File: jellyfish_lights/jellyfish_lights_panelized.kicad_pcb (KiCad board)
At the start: 2 copper layers, 94 x 94 mm, 528 parts, among them Q1 AO3400A, SW1 tilt switch, SW2 tilt switch, U1 SN74LVC1G14DBVR

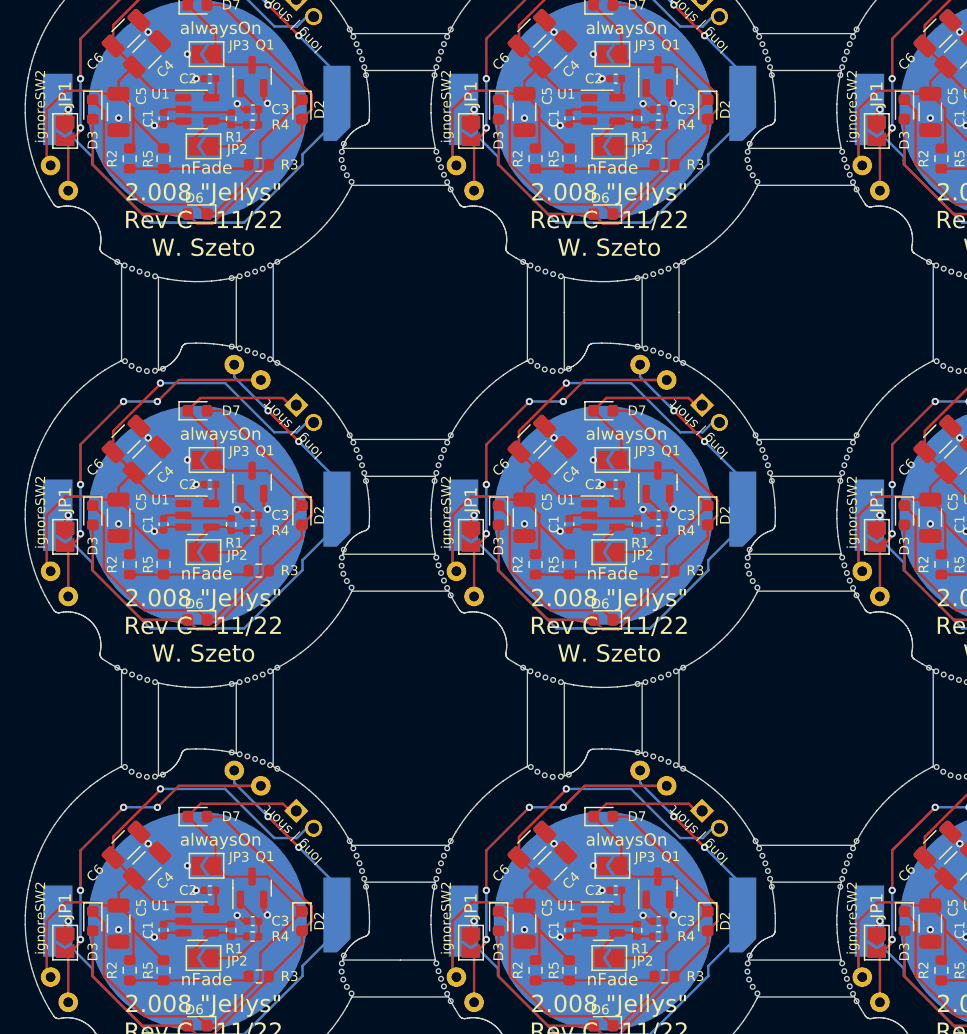
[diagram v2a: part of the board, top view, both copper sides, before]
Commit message: changed jumper to 0R resistor for ignoreSW2
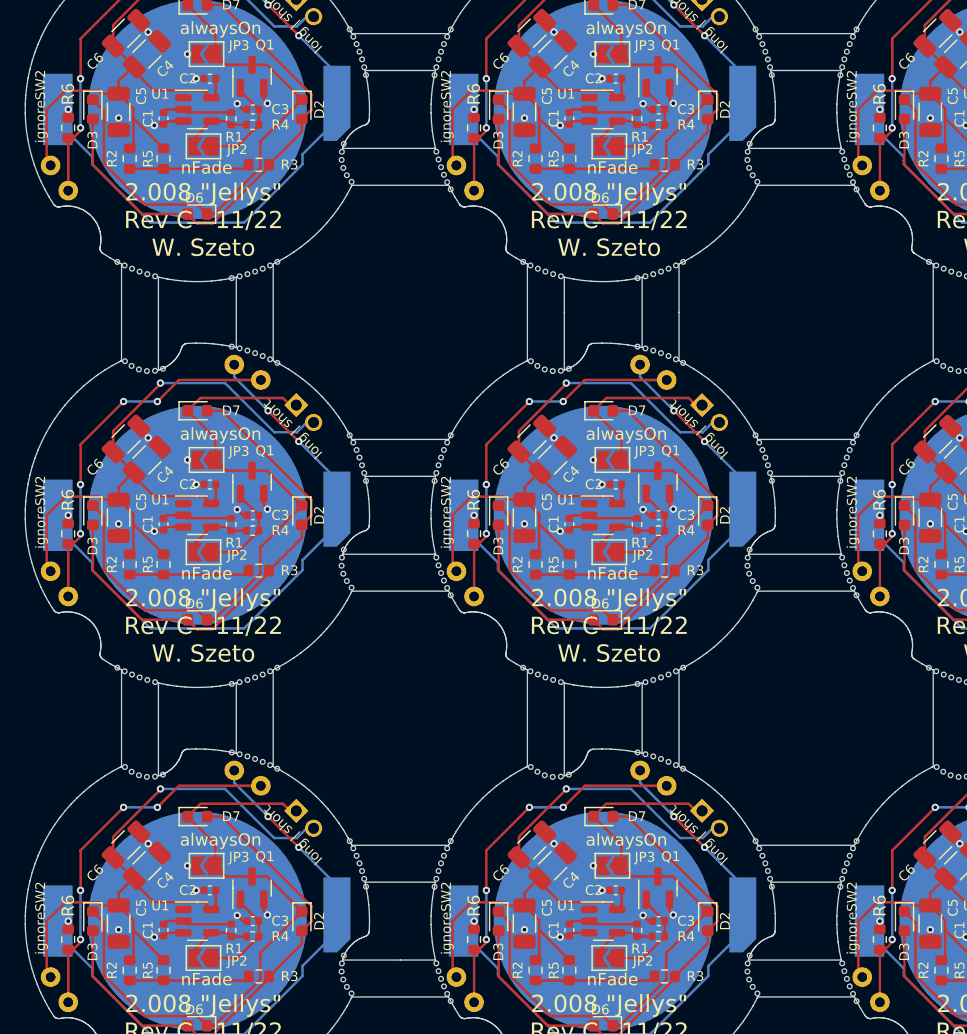
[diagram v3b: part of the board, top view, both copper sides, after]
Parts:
- removed JP1 (x9): oneTiltSw, Jumper:SolderJumper-2_P1.3mm_Open_TrianglePad1.0x1.5mm
- added R6: 0R, Resistor_SMD:R_0603_1608Metric, F.Cu at (72.5, 84.5)
- added R6: 0R, Resistor_SMD:R_0603_1608Metric, F.Cu at (39.5, 84.5)
- added R6: 0R, Resistor_SMD:R_0603_1608Metric, F.Cu at (72.5, 117.5)
- added R6: 0R, Resistor_SMD:R_0603_1608Metric, F.Cu at (105.5, 51.5)
- added R6: 0R, Resistor_SMD:R_0603_1608Metric, F.Cu at (39.5, 117.5)
- added R6: 0R, Resistor_SMD:R_0603_1608Metric, F.Cu at (39.5, 51.5)
- added R6: 0R, Resistor_SMD:R_0603_1608Metric, F.Cu at (105.5, 117.5)
- added R6: 0R, Resistor_SMD:R_0603_1608Metric, F.Cu at (105.5, 84.5)
- added R6: 0R, Resistor_SMD:R_0603_1608Metric, F.Cu at (72.5, 51.5)
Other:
- board text added: "Rev C"

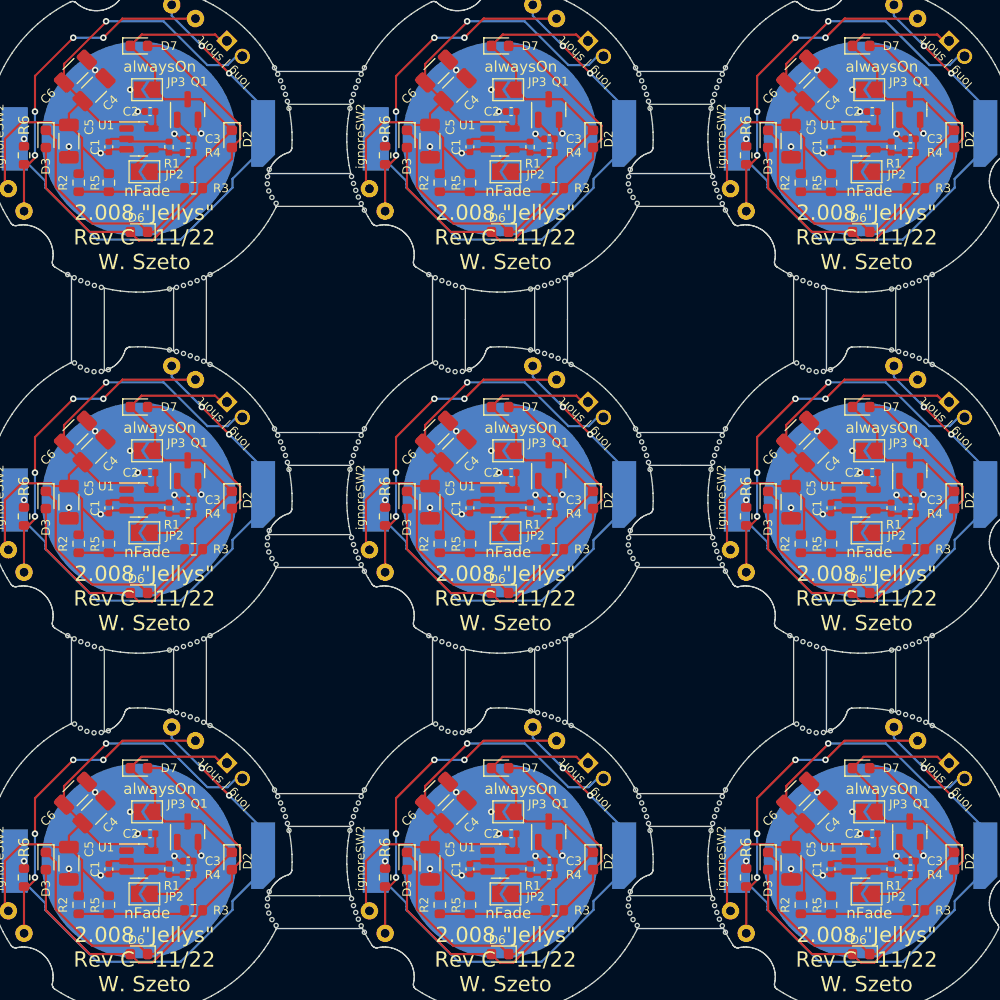
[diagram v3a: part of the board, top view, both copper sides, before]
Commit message: Updated BOM/POS file
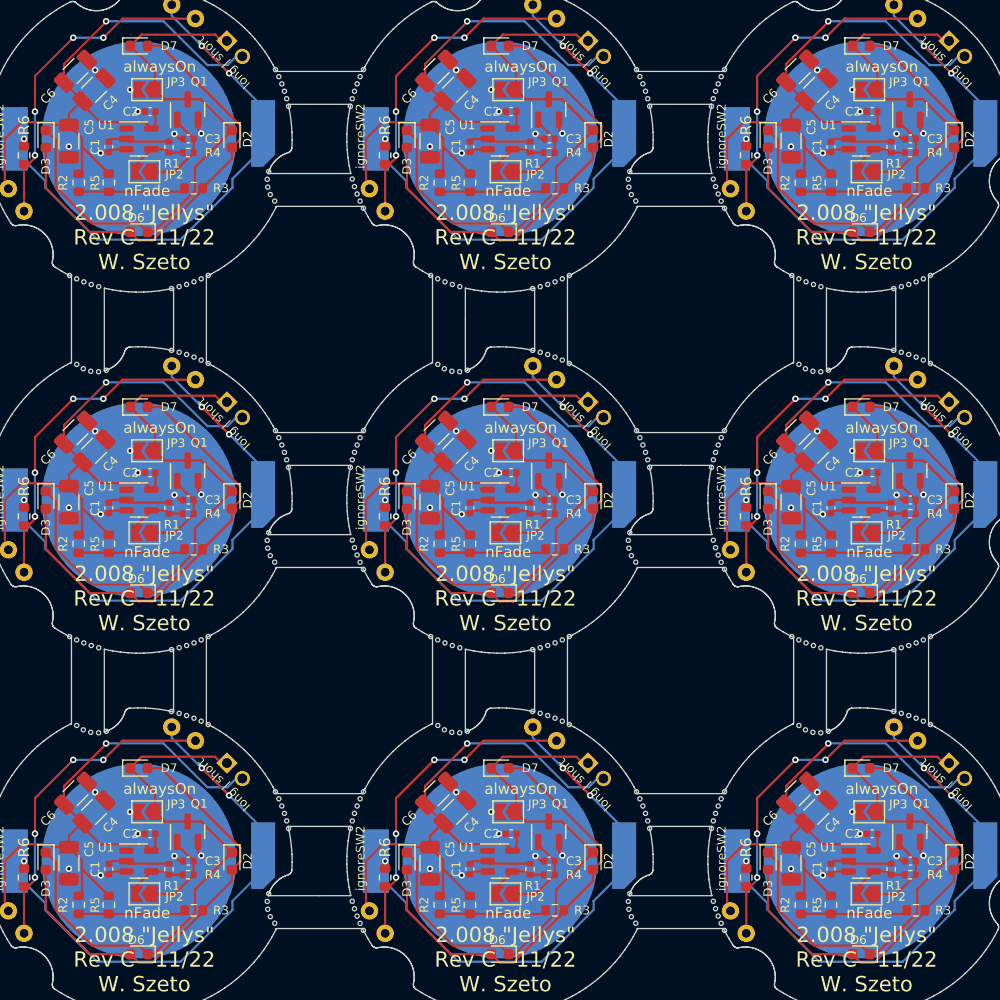
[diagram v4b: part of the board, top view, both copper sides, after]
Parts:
- removed the REF** at (76.5, 62.4)
- removed the REF** at (87.7, 102.8)
- removed the REF** at (121.9, 62.7)
- removed the REF** at (44.1, 70.5)
- removed the REF** at (122.5, 103.6)
- removed the REF** at (118.8, 102.3)
- removed the REF** at (69.6, 45.9)
- removed the REF** at (102.4, 46.6)
- removed the REF** at (119.4, 69.4)
- removed the REF** at (96.2, 111.3)
- removed the REF** at (70.3, 121.9)
- removed the REF** at (102.3, 47.2)
- removed the REF** at (63.4, 45.9)
- removed the REF** at (111.3, 63.2)
- removed the REF** at (78.2, 104.1)
- removed the REF** at (69.3, 80.2)
- removed the REF** at (46.6, 96.6)
- removed the REF** at (78.9, 63.4)
- removed the REF** at (111.9, 104.3)
- removed the REF** at (120.1, 102.6)
- removed the REF** at (96.7, 47.2)
- removed the REF** at (45.9, 96.4)
- removed the REF** at (96.2, 45.3)
- removed the REF** at (86.4, 96.6)
- removed the REF** at (78.3, 96.2)
- removed the REF** at (102.6, 78.9)
- removed the REF** at (118.8, 96.7)
- removed the REF** at (78.9, 96.4)
- removed the REF** at (79.6, 96.6)
- removed the REF** at (96.7, 80.2)
- removed the REF** at (54.7, 63.2)
- removed the REF** at (55.3, 70.1)
- removed the REF** at (87.1, 102.6)
- removed the REF** at (103.3, 77.1)
- removed the REF** at (88.9, 70.3)
- removed the REF** at (61.9, 120.8)
- removed the REF** at (70.6, 76.5)
- removed the REF** at (63.2, 111.3)
- removed the REF** at (94.8, 119.4)
- removed the REF** at (94.9, 87.8)
- removed the REF** at (89.5, 70.6)
- removed the REF** at (63.4, 111.9)
- removed the REF** at (88.3, 70.1)
- removed the REF** at (94.9, 120.8)
- removed the REF** at (94.7, 54.1)
- removed the REF** at (94.9, 85.8)
- removed the REF** at (70.0, 44.7)
- removed the REF** at (70.3, 44.1)
- removed the REF** at (79.6, 63.6)
- removed the REF** at (96.4, 45.9)
- removed the REF** at (103.3, 110.1)
- removed the REF** at (69.8, 54.7)
- removed the REF** at (54.1, 96.4)
- removed the REF** at (61.9, 118.8)
- removed the REF** at (78.2, 71.1)
- removed the REF** at (77.7, 103.9)
- removed the REF** at (52.8, 96.7)
- removed the REF** at (80.2, 71.1)
- removed the REF** at (44.7, 95.9)
- removed the REF** at (103.3, 44.1)
- removed the REF** at (88.3, 103.1)
- removed the REF** at (61.9, 54.8)
- removed the REF** at (95.7, 110.1)
- removed the REF** at (54.1, 69.6)
- removed the REF** at (94.7, 120.1)
- removed the REF** at (44.1, 103.5)
- removed the REF** at (47.2, 71.1)
- removed the REF** at (45.9, 104.3)
- removed the REF** at (61.8, 86.4)
- removed the REF** at (112.6, 104.2)
- removed the REF** at (44.7, 62.9)
- removed the REF** at (109.5, 62.4)
- removed the REF** at (69.6, 87.1)
- removed the REF** at (70.6, 122.5)
- removed the REF** at (122.5, 95.4)
- removed the REF** at (95.2, 121.3)
- removed the REF** at (103.6, 76.5)
- removed the REF** at (69.8, 120.7)
- removed the REF** at (96.6, 46.6)
- removed the REF** at (94.9, 52.8)
- removed the REF** at (96.6, 79.6)
- removed the REF** at (55.9, 70.3)
- removed the REF** at (70.1, 55.3)
- removed the REF** at (61.7, 87.1)
- removed the REF** at (52.8, 63.7)
- removed the REF** at (103.6, 56.5)
- removed the REF** at (45.3, 63.2)
- removed the REF** at (102.6, 54.1)
- removed the REF** at (77.1, 62.7)
- removed the REF** at (45.3, 96.2)
- removed the REF** at (70.6, 43.5)
- removed the REF** at (120.7, 102.8)
- removed the REF** at (103.0, 44.7)
- removed the REF** at (63.2, 78.3)
- removed the REF** at (69.4, 112.6)
- removed the REF** at (61.8, 53.4)
- removed the REF** at (55.9, 103.3)
- removed the REF** at (102.8, 78.3)
- removed the REF** at (54.1, 63.4)
- removed the REF** at (70.1, 88.3)
- removed the REF** at (62.9, 77.7)
- removed the REF** at (85.8, 102.3)
- removed the REF** at (70.3, 88.9)
- removed the REF** at (62.4, 76.5)
- removed the REF** at (78.9, 104.3)
- removed the REF** at (69.3, 113.2)
- removed the REF** at (103.6, 122.5)
- removed the REF** at (96.6, 112.6)
- removed the REF** at (70.3, 77.1)
- removed the REF** at (88.9, 95.7)
- removed the REF** at (45.2, 71.1)
- removed the REF** at (109.5, 95.4)
- removed the REF** at (69.4, 79.6)
- removed the REF** at (69.6, 111.9)
- removed the REF** at (61.9, 87.8)
- removed the REF** at (113.2, 71.1)
- removed the REF** at (120.1, 96.4)
- removed the REF** at (95.5, 55.9)
- removed the REF** at (113.2, 104.1)
- removed the REF** at (69.3, 47.2)
- removed the REF** at (103.0, 77.7)
- removed the REF** at (102.6, 111.9)
- removed the REF** at (111.9, 63.4)
- removed the REF** at (78.3, 63.2)
- removed the REF** at (62.9, 44.7)
- removed the REF** at (95.9, 77.7)
- removed the REF** at (119.4, 63.6)
- removed the REF** at (61.7, 120.1)
- removed the REF** at (95.9, 44.7)
- removed the REF** at (69.4, 53.4)
- removed the REF** at (43.5, 62.4)
- removed the REF** at (77.1, 95.7)
- removed the REF** at (102.8, 45.3)
- removed the REF** at (85.8, 63.7)
- removed the REF** at (103.1, 55.3)
- removed the REF** at (102.8, 54.7)
- removed the REF** at (95.9, 110.7)
- removed the REF** at (56.5, 70.6)
- removed the REF** at (86.4, 63.6)
- removed the REF** at (62.7, 44.1)
- removed the REF** at (96.7, 113.2)
- removed the REF** at (77.7, 70.9)
- removed the REF** at (94.8, 53.4)
- removed the REF** at (102.4, 86.4)
- removed the REF** at (55.3, 96.0)
- removed the REF** at (45.2, 104.1)
- removed the REF** at (86.4, 69.4)
- removed the REF** at (63.2, 45.3)
- removed the REF** at (121.3, 96.0)
- removed the REF** at (56.5, 95.4)
- removed the REF** at (111.9, 96.4)
- removed the REF** at (102.3, 80.2)
- removed the REF** at (112.6, 63.6)
- removed the REF** at (120.7, 96.2)
- removed the REF** at (46.6, 71.2)
- removed the REF** at (103.3, 88.9)
- removed the REF** at (55.9, 62.7)
- removed the REF** at (110.7, 62.9)
- removed the REF** at (95.7, 77.1)
- removed the REF** at (62.7, 110.1)
- removed the REF** at (102.4, 119.4)
- removed the REF** at (54.7, 96.2)
- removed the REF** at (89.5, 95.4)
- removed the REF** at (119.4, 96.6)
- removed the REF** at (102.6, 87.1)
- removed the REF** at (120.1, 69.6)
- removed the REF** at (53.4, 69.4)
- removed the REF** at (111.2, 71.1)
- removed the REF** at (61.7, 54.1)
- removed the REF** at (70.0, 77.7)
- removed the REF** at (112.6, 96.6)
- removed the REF** at (118.8, 69.3)
- removed the REF** at (63.7, 113.2)
- removed the REF** at (69.6, 54.1)
- removed the REF** at (70.6, 89.5)
- removed the REF** at (89.5, 62.4)
- removed the REF** at (77.7, 95.9)
- removed the REF** at (120.7, 63.2)
- removed the REF** at (118.8, 63.7)
- removed the REF** at (52.8, 102.3)
- removed the REF** at (96.4, 78.9)
- removed the REF** at (53.4, 102.4)
- removed the REF** at (63.6, 112.6)
- removed the REF** at (102.4, 53.4)
- removed the REF** at (69.4, 46.6)
- removed the REF** at (119.4, 102.4)
- removed the REF** at (63.6, 46.6)
- removed the REF** at (121.9, 70.3)
- removed the REF** at (53.4, 96.6)
- removed the REF** at (95.4, 109.5)
- removed the REF** at (69.4, 86.4)
- removed the REF** at (53.4, 63.6)
- removed the REF** at (103.1, 88.3)
- removed the REF** at (78.9, 71.3)
- removed the REF** at (95.4, 76.5)
- removed the REF** at (69.6, 120.1)
- removed the REF** at (62.2, 55.3)
- removed the REF** at (63.4, 78.9)
- removed the REF** at (121.3, 70.1)
- removed the REF** at (69.8, 87.7)
- removed the REF** at (63.6, 79.6)
- removed the REF** at (45.9, 63.4)
- removed the REF** at (70.6, 109.5)
- removed the REF** at (80.2, 104.1)
- removed the REF** at (96.2, 78.3)
- removed the REF** at (46.6, 63.6)
- removed the REF** at (110.7, 95.9)
- removed the REF** at (44.1, 62.7)
- removed the REF** at (103.6, 43.5)
- removed the REF** at (46.6, 104.2)
- removed the REF** at (76.5, 95.4)
- removed the REF** at (103.3, 55.9)
- removed the REF** at (94.7, 87.1)
- removed the REF** at (102.4, 112.6)
- removed the REF** at (87.7, 96.2)
- removed the REF** at (89.5, 103.6)
- removed the REF** at (103.1, 121.3)
- removed the REF** at (87.1, 69.6)
- removed the REF** at (87.1, 96.4)
- removed the REF** at (69.8, 78.3)
- removed the REF** at (122.5, 70.6)
- removed the REF** at (44.1, 95.7)
- removed the REF** at (77.7, 62.9)
- removed the REF** at (56.5, 103.6)
- removed the REF** at (54.1, 102.6)
- removed the REF** at (87.7, 69.8)
- removed the REF** at (102.8, 87.7)
- removed the REF** at (102.6, 45.9)
- removed the REF** at (77.1, 70.5)
- removed the REF** at (94.9, 54.8)
- removed the REF** at (95.7, 44.1)
- removed the REF** at (102.4, 79.6)
- removed the REF** at (94.8, 86.4)
- removed the REF** at (95.5, 121.9)
- removed the REF** at (88.3, 63.0)
- removed the REF** at (121.3, 103.1)
- removed the REF** at (95.2, 55.3)
- removed the REF** at (55.9, 95.7)
- removed the REF** at (61.9, 85.8)
- removed the REF** at (70.6, 56.5)
- removed the REF** at (102.6, 120.1)
- removed the REF** at (61.8, 119.4)
- removed the REF** at (121.9, 95.7)
- removed the REF** at (85.8, 96.7)
- removed the REF** at (62.2, 88.3)
- removed the REF** at (110.7, 70.9)
- removed the REF** at (62.9, 110.7)
- removed the REF** at (88.3, 96.0)
- removed the REF** at (88.9, 103.3)
- removed the REF** at (61.9, 52.8)
- removed the REF** at (87.7, 63.2)
- removed the REF** at (111.3, 96.2)
- removed the REF** at (111.2, 104.1)
- removed the REF** at (79.6, 104.2)
- removed the REF** at (102.8, 111.3)
- removed the REF** at (102.8, 120.7)
- removed the REF** at (62.5, 55.9)
- removed the REF** at (95.4, 43.5)
- removed the REF** at (69.6, 78.9)
- removed the REF** at (62.7, 77.1)
- removed the REF** at (103.0, 110.7)
- removed the REF** at (102.3, 113.2)
- removed the REF** at (95.5, 88.9)
- removed the REF** at (95.2, 88.3)
- removed the REF** at (85.8, 69.3)
- removed the REF** at (44.7, 70.9)
- removed the REF** at (55.3, 63.0)
- removed the REF** at (96.4, 111.9)
- removed the REF** at (55.3, 103.1)
- removed the REF** at (70.0, 110.7)
- removed the REF** at (70.1, 121.3)
- removed the REF** at (44.7, 103.9)
- removed the REF** at (88.9, 62.7)
- removed the REF** at (62.2, 121.3)
- removed the REF** at (103.3, 121.9)
- removed the REF** at (110.1, 103.5)
- removed the REF** at (47.2, 104.1)
- removed the REF** at (110.1, 70.5)
- removed the REF** at (110.1, 95.7)
- removed the REF** at (62.5, 121.9)
- removed the REF** at (121.3, 63.0)
- removed the REF** at (87.1, 63.4)
- removed the REF** at (69.8, 45.3)
- removed the REF** at (43.5, 95.4)
- removed the REF** at (70.3, 55.9)
- removed the REF** at (70.3, 110.1)
- removed the REF** at (63.7, 47.2)
- removed the REF** at (63.7, 80.2)
- removed the REF** at (110.7, 103.9)
- removed the REF** at (94.9, 118.8)
- removed the REF** at (111.9, 71.3)
- removed the REF** at (52.8, 69.3)
- removed the REF** at (120.7, 69.8)
- removed the REF** at (45.9, 71.3)
- removed the REF** at (79.6, 71.2)
- removed the REF** at (69.4, 119.4)
- removed the REF** at (86.4, 102.4)
- removed the REF** at (120.1, 63.4)
- removed the REF** at (56.5, 62.4)
- removed the REF** at (54.7, 69.8)
- removed the REF** at (62.5, 88.9)
- removed the REF** at (103.6, 89.5)
- removed the REF** at (110.1, 62.7)
- removed the REF** at (103.6, 109.5)
- removed the REF** at (121.9, 103.3)
- removed the REF** at (122.5, 62.4)
- removed the REF** at (62.4, 109.5)
- removed the REF** at (62.4, 43.5)
- removed the REF** at (112.6, 71.2)
- removed the REF** at (77.1, 103.5)
- removed the REF** at (54.7, 102.8)
- removed the REF** at (69.8, 111.3)
- added REF**: NPTH, NPTH, F.Cu at (103.2, 110.3)
- added REF**: NPTH, NPTH, F.Cu at (95.5, 76.7)
- added REF**: NPTH, NPTH, F.Cu at (113.0, 71.1)
- added REF**: NPTH, NPTH, F.Cu at (79.3, 104.3)
- added REF**: NPTH, NPTH, F.Cu at (61.8, 87.4)
- added REF**: NPTH, NPTH, F.Cu at (102.7, 45.6)
- added REF**: NPTH, NPTH, F.Cu at (69.7, 111.6)
- added REF**: NPTH, NPTH, F.Cu at (45.6, 71.2)
- added REF**: NPTH, NPTH, F.Cu at (80.0, 104.1)
- added REF**: NPTH, NPTH, F.Cu at (121.0, 63.1)
- added REF**: NPTH, NPTH, F.Cu at (70.2, 55.7)
- added REF**: NPTH, NPTH, F.Cu at (43.7, 62.5)
- added REF**: NPTH, NPTH, F.Cu at (44.3, 62.8)
- added REF**: NPTH, NPTH, F.Cu at (102.9, 55.0)
- added REF**: NPTH, NPTH, F.Cu at (70.5, 122.3)
- added REF**: NPTH, NPTH, F.Cu at (86.7, 96.5)
- added REF**: NPTH, NPTH, F.Cu at (121.7, 62.8)
- added REF**: NPTH, NPTH, F.Cu at (63.5, 79.3)
- added REF**: NPTH, NPTH, F.Cu at (96.3, 78.6)
- added REF**: NPTH, NPTH, F.Cu at (96.3, 45.6)
- added REF**: NPTH, NPTH, F.Cu at (63.7, 113.0)
- added REF**: NPTH, NPTH, F.Cu at (110.9, 104.0)
- added REF**: NPTH, NPTH, F.Cu at (119.7, 96.5)
- added REF**: NPTH, NPTH, F.Cu at (94.8, 54.4)
- added REF**: NPTH, NPTH, F.Cu at (87.4, 63.3)
- added REF**: NPTH, NPTH, F.Cu at (87.4, 96.3)
- added REF**: NPTH, NPTH, F.Cu at (102.3, 47.0)
- added REF**: NPTH, NPTH, F.Cu at (96.5, 79.3)
- added REF**: NPTH, NPTH, F.Cu at (89.3, 103.5)
- added REF**: NPTH, NPTH, F.Cu at (102.7, 54.4)
- added REF**: NPTH, NPTH, F.Cu at (102.9, 45.0)
- added REF**: NPTH, NPTH, F.Cu at (95.5, 43.7)
- added REF**: NPTH, NPTH, F.Cu at (70.2, 121.7)
- added REF**: NPTH, NPTH, F.Cu at (77.9, 71.0)
- added REF**: NPTH, NPTH, F.Cu at (62.5, 76.7)
- added REF**: NPTH, NPTH, F.Cu at (89.3, 62.5)
- added REF**: NPTH, NPTH, F.Cu at (53.7, 96.5)
- added REF**: NPTH, NPTH, F.Cu at (102.5, 79.3)
- added REF**: NPTH, NPTH, F.Cu at (95.8, 77.3)
- added REF**: NPTH, NPTH, F.Cu at (63.7, 47.0)
- added REF**: NPTH, NPTH, F.Cu at (70.2, 110.3)
- added REF**: NPTH, NPTH, F.Cu at (55.7, 70.2)
- added REF**: NPTH, NPTH, F.Cu at (95.8, 110.3)
- added REF**: NPTH, NPTH, F.Cu at (46.3, 63.5)
- added REF**: NPTH, NPTH, F.Cu at (103.5, 76.7)
- added REF**: NPTH, NPTH, F.Cu at (96.7, 47.0)
- added REF**: NPTH, NPTH, F.Cu at (69.9, 111.0)
- added REF**: NPTH, NPTH, F.Cu at (78.6, 96.3)
- added REF**: NPTH, NPTH, F.Cu at (53.7, 63.5)
- added REF**: NPTH, NPTH, F.Cu at (69.3, 80.0)
- added REF**: NPTH, NPTH, F.Cu at (79.3, 96.5)
- added REF**: NPTH, NPTH, F.Cu at (69.9, 55.0)
- added REF**: NPTH, NPTH, F.Cu at (111.6, 104.2)
- added REF**: NPTH, NPTH, F.Cu at (45.6, 96.3)
- added REF**: NPTH, NPTH, F.Cu at (121.0, 96.1)
- added REF**: NPTH, NPTH, F.Cu at (62.8, 77.3)
- added REF**: NPTH, NPTH, F.Cu at (111.6, 96.3)
- added REF**: NPTH, NPTH, F.Cu at (62.4, 88.7)
- added REF**: NPTH, NPTH, F.Cu at (121.7, 95.8)
- added REF**: NPTH, NPTH, F.Cu at (69.5, 53.7)
- added REF**: NPTH, NPTH, F.Cu at (77.3, 103.6)
- added REF**: NPTH, NPTH, F.Cu at (96.1, 78.0)
- added REF**: NPTH, NPTH, F.Cu at (78.0, 63.1)
- added REF**: NPTH, NPTH, F.Cu at (54.4, 102.7)
- added REF**: NPTH, NPTH, F.Cu at (121.7, 70.2)
- added REF**: NPTH, NPTH, F.Cu at (54.4, 96.3)
- added REF**: NPTH, NPTH, F.Cu at (88.7, 95.8)
- added REF**: NPTH, NPTH, F.Cu at (43.7, 95.5)
- added REF**: NPTH, NPTH, F.Cu at (61.9, 53.0)
- added REF**: NPTH, NPTH, F.Cu at (55.0, 102.9)
- added REF**: NPTH, NPTH, F.Cu at (61.8, 54.4)
- added REF**: NPTH, NPTH, F.Cu at (53.0, 96.7)
- added REF**: NPTH, NPTH, F.Cu at (62.4, 55.7)
- added REF**: NPTH, NPTH, F.Cu at (103.5, 89.3)
- added REF**: NPTH, NPTH, F.Cu at (119.7, 69.5)
- added REF**: NPTH, NPTH, F.Cu at (69.5, 46.3)
- added REF**: NPTH, NPTH, F.Cu at (110.3, 95.8)
- added REF**: NPTH, NPTH, F.Cu at (88.0, 96.1)
- added REF**: NPTH, NPTH, F.Cu at (70.5, 76.7)
- added REF**: NPTH, NPTH, F.Cu at (102.3, 80.0)
- added REF**: NPTH, NPTH, F.Cu at (70.2, 44.3)
- added REF**: NPTH, NPTH, F.Cu at (119.0, 69.3)
- added REF**: NPTH, NPTH, F.Cu at (94.9, 53.0)
- added REF**: NPTH, NPTH, F.Cu at (63.1, 111.0)
- added REF**: NPTH, NPTH, F.Cu at (46.3, 71.3)
- added REF**: NPTH, NPTH, F.Cu at (76.7, 62.5)
- added REF**: NPTH, NPTH, F.Cu at (63.3, 111.6)
- added REF**: NPTH, NPTH, F.Cu at (119.0, 102.3)
- added REF**: NPTH, NPTH, F.Cu at (76.7, 95.5)
- added REF**: NPTH, NPTH, F.Cu at (96.1, 111.0)
- added REF**: NPTH, NPTH, F.Cu at (110.3, 103.6)
- added REF**: NPTH, NPTH, F.Cu at (78.6, 104.2)
- added REF**: NPTH, NPTH, F.Cu at (45.0, 96.1)
- added REF**: NPTH, NPTH, F.Cu at (45.0, 63.1)
- added REF**: NPTH, NPTH, F.Cu at (121.7, 103.2)
- added REF**: NPTH, NPTH, F.Cu at (87.4, 69.7)
- added REF**: NPTH, NPTH, F.Cu at (77.3, 62.8)
- added REF**: NPTH, NPTH, F.Cu at (53.0, 69.3)
- added REF**: NPTH, NPTH, F.Cu at (62.0, 88.1)
- added REF**: NPTH, NPTH, F.Cu at (77.3, 95.8)
- added REF**: NPTH, NPTH, F.Cu at (94.9, 119.0)
- added REF**: NPTH, NPTH, F.Cu at (63.5, 112.3)
- added REF**: NPTH, NPTH, F.Cu at (69.9, 121.0)
- added REF**: NPTH, NPTH, F.Cu at (78.6, 71.2)
- added REF**: NPTH, NPTH, F.Cu at (55.7, 95.8)
- added REF**: NPTH, NPTH, F.Cu at (70.5, 56.3)
- added REF**: NPTH, NPTH, F.Cu at (62.0, 55.1)
- added REF**: NPTH, NPTH, F.Cu at (103.2, 88.7)
- added REF**: NPTH, NPTH, F.Cu at (119.7, 63.5)
- added REF**: NPTH, NPTH, F.Cu at (78.0, 96.1)
- added REF**: NPTH, NPTH, F.Cu at (88.0, 69.9)
- added REF**: NPTH, NPTH, F.Cu at (110.3, 62.8)
- added REF**: NPTH, NPTH, F.Cu at (103.5, 122.3)
- added REF**: NPTH, NPTH, F.Cu at (94.9, 86.0)
- added REF**: NPTH, NPTH, F.Cu at (88.0, 102.9)
- added REF**: NPTH, NPTH, F.Cu at (69.9, 78.0)
- added REF**: NPTH, NPTH, F.Cu at (86.7, 63.5)
- added REF**: NPTH, NPTH, F.Cu at (119.7, 102.5)
- added REF**: NPTH, NPTH, F.Cu at (96.5, 112.3)
- added REF**: NPTH, NPTH, F.Cu at (69.7, 120.4)
- added REF**: NPTH, NPTH, F.Cu at (62.8, 110.3)
- added REF**: NPTH, NPTH, F.Cu at (69.5, 79.3)
- added REF**: NPTH, NPTH, F.Cu at (95.0, 121.1)
- added REF**: NPTH, NPTH, F.Cu at (56.3, 70.5)
- added REF**: NPTH, NPTH, F.Cu at (79.3, 63.5)
- added REF**: NPTH, NPTH, F.Cu at (110.9, 71.0)
- added REF**: NPTH, NPTH, F.Cu at (61.8, 120.4)
- added REF**: NPTH, NPTH, F.Cu at (96.7, 113.0)
- added REF**: NPTH, NPTH, F.Cu at (102.7, 87.4)
- added REF**: NPTH, NPTH, F.Cu at (69.5, 86.7)
- added REF**: NPTH, NPTH, F.Cu at (89.3, 70.5)
- added REF**: NPTH, NPTH, F.Cu at (95.4, 88.7)
- added REF**: NPTH, NPTH, F.Cu at (44.3, 103.6)
- added REF**: NPTH, NPTH, F.Cu at (102.5, 112.3)
- added REF**: NPTH, NPTH, F.Cu at (86.0, 96.7)
- added REF**: NPTH, NPTH, F.Cu at (111.0, 63.1)
- added REF**: NPTH, NPTH, F.Cu at (44.3, 95.8)
- added REF**: NPTH, NPTH, F.Cu at (88.0, 63.1)
- added REF**: NPTH, NPTH, F.Cu at (61.7, 53.7)
- added REF**: NPTH, NPTH, F.Cu at (70.5, 109.7)
- added REF**: NPTH, NPTH, F.Cu at (96.1, 45.0)
- added REF**: NPTH, NPTH, F.Cu at (69.3, 113.0)
- added REF**: NPTH, NPTH, F.Cu at (45.6, 104.2)
- added REF**: NPTH, NPTH, F.Cu at (110.3, 70.6)
- added REF**: NPTH, NPTH, F.Cu at (88.7, 62.8)
- added REF**: NPTH, NPTH, F.Cu at (61.9, 119.0)
- added REF**: NPTH, NPTH, F.Cu at (102.5, 86.7)
- added REF**: NPTH, NPTH, F.Cu at (112.3, 71.3)
- added REF**: NPTH, NPTH, F.Cu at (55.0, 69.9)
- added REF**: NPTH, NPTH, F.Cu at (96.5, 46.3)
- added REF**: NPTH, NPTH, F.Cu at (95.4, 121.7)
- added REF**: NPTH, NPTH, F.Cu at (44.9, 71.0)
- added REF**: NPTH, NPTH, F.Cu at (102.7, 111.6)
- added REF**: NPTH, NPTH, F.Cu at (102.5, 46.3)
- added REF**: NPTH, NPTH, F.Cu at (102.3, 113.0)
- added REF**: NPTH, NPTH, F.Cu at (54.4, 63.3)
- added REF**: NPTH, NPTH, F.Cu at (120.4, 96.3)
- added REF**: NPTH, NPTH, F.Cu at (63.3, 45.6)
- added REF**: NPTH, NPTH, F.Cu at (69.7, 45.6)
- added REF**: NPTH, NPTH, F.Cu at (111.0, 96.1)
- added REF**: NPTH, NPTH, F.Cu at (121.0, 102.9)
- added REF**: NPTH, NPTH, F.Cu at (94.8, 87.4)
- added REF**: NPTH, NPTH, F.Cu at (87.4, 102.7)
- added REF**: NPTH, NPTH, F.Cu at (109.7, 62.5)
- added REF**: NPTH, NPTH, F.Cu at (86.0, 102.3)
- added REF**: NPTH, NPTH, F.Cu at (88.7, 103.2)
- added REF**: NPTH, NPTH, F.Cu at (56.3, 62.5)
- added REF**: NPTH, NPTH, F.Cu at (69.9, 88.0)
- added REF**: NPTH, NPTH, F.Cu at (120.4, 63.3)
- added REF**: NPTH, NPTH, F.Cu at (103.2, 121.7)
- added REF**: NPTH, NPTH, F.Cu at (44.9, 104.0)
- added REF**: NPTH, NPTH, F.Cu at (120.4, 102.7)
- added REF**: NPTH, NPTH, F.Cu at (95.5, 109.7)
- added REF**: NPTH, NPTH, F.Cu at (103.5, 56.3)
- added REF**: NPTH, NPTH, F.Cu at (69.5, 112.3)
- added REF**: NPTH, NPTH, F.Cu at (77.9, 104.0)
- added REF**: NPTH, NPTH, F.Cu at (94.7, 119.7)
- added REF**: NPTH, NPTH, F.Cu at (79.3, 71.3)
- added REF**: NPTH, NPTH, F.Cu at (46.3, 96.5)
- added REF**: NPTH, NPTH, F.Cu at (56.3, 95.5)
- added REF**: NPTH, NPTH, F.Cu at (95.4, 55.7)
- added REF**: NPTH, NPTH, F.Cu at (103.2, 77.3)
- added REF**: NPTH, NPTH, F.Cu at (69.7, 87.4)
- added REF**: NPTH, NPTH, F.Cu at (102.5, 53.7)
- added REF**: NPTH, NPTH, F.Cu at (102.7, 120.4)
- added REF**: NPTH, NPTH, F.Cu at (63.5, 46.3)
- added REF**: NPTH, NPTH, F.Cu at (112.3, 63.5)
- added REF**: NPTH, NPTH, F.Cu at (111.6, 63.3)
- added REF**: NPTH, NPTH, F.Cu at (56.3, 103.5)
- added REF**: NPTH, NPTH, F.Cu at (102.7, 78.6)
- added REF**: NPTH, NPTH, F.Cu at (63.7, 80.0)
- added REF**: NPTH, NPTH, F.Cu at (112.3, 96.5)
- added REF**: NPTH, NPTH, F.Cu at (53.0, 102.3)
- added REF**: NPTH, NPTH, F.Cu at (102.9, 121.0)
- added REF**: NPTH, NPTH, F.Cu at (119.0, 96.7)
- added REF**: NPTH, NPTH, F.Cu at (53.7, 102.5)
- added REF**: NPTH, NPTH, F.Cu at (86.0, 69.3)
- added REF**: NPTH, NPTH, F.Cu at (62.5, 43.7)
- added REF**: NPTH, NPTH, F.Cu at (46.3, 104.3)
- added REF**: NPTH, NPTH, F.Cu at (102.9, 78.0)
- added REF**: NPTH, NPTH, F.Cu at (103.5, 43.7)
- added REF**: NPTH, NPTH, F.Cu at (88.7, 70.2)
- added REF**: NPTH, NPTH, F.Cu at (62.8, 44.3)
- added REF**: NPTH, NPTH, F.Cu at (95.0, 88.1)
- added REF**: NPTH, NPTH, F.Cu at (55.7, 62.8)
- added REF**: NPTH, NPTH, F.Cu at (70.2, 88.7)
- added REF**: NPTH, NPTH, F.Cu at (69.7, 78.6)
- added REF**: NPTH, NPTH, F.Cu at (47.0, 71.1)
- added REF**: NPTH, NPTH, F.Cu at (122.3, 103.5)
- added REF**: NPTH, NPTH, F.Cu at (54.4, 69.7)
- added REF**: NPTH, NPTH, F.Cu at (55.0, 96.1)
- added REF**: NPTH, NPTH, F.Cu at (113.0, 104.1)
- added REF**: NPTH, NPTH, F.Cu at (120.4, 69.7)
- added REF**: NPTH, NPTH, F.Cu at (63.3, 78.6)
- added REF**: NPTH, NPTH, F.Cu at (47.0, 104.1)
- added REF**: NPTH, NPTH, F.Cu at (94.7, 86.7)
- added REF**: NPTH, NPTH, F.Cu at (122.3, 62.5)
- added REF**: NPTH, NPTH, F.Cu at (55.7, 103.2)
- added REF**: NPTH, NPTH, F.Cu at (94.7, 53.7)
- added REF**: NPTH, NPTH, F.Cu at (103.2, 44.3)
- added REF**: NPTH, NPTH, F.Cu at (89.3, 95.5)
- added REF**: NPTH, NPTH, F.Cu at (95.0, 55.1)
- added REF**: NPTH, NPTH, F.Cu at (121.0, 69.9)
- added REF**: NPTH, NPTH, F.Cu at (53.7, 69.5)
- added REF**: NPTH, NPTH, F.Cu at (112.3, 104.3)
- added REF**: NPTH, NPTH, F.Cu at (53.0, 63.7)
- added REF**: NPTH, NPTH, F.Cu at (69.9, 45.0)
- added REF**: NPTH, NPTH, F.Cu at (86.7, 69.5)
- added REF**: NPTH, NPTH, F.Cu at (78.6, 63.3)
- added REF**: NPTH, NPTH, F.Cu at (95.8, 44.3)
- added REF**: NPTH, NPTH, F.Cu at (86.7, 102.5)
- added REF**: NPTH, NPTH, F.Cu at (61.7, 86.7)
- added REF**: NPTH, NPTH, F.Cu at (122.3, 95.5)
- added REF**: NPTH, NPTH, F.Cu at (69.3, 47.0)
- added REF**: NPTH, NPTH, F.Cu at (109.7, 95.5)
- added REF**: NPTH, NPTH, F.Cu at (103.5, 109.7)
- added REF**: NPTH, NPTH, F.Cu at (62.4, 121.7)
- added REF**: NPTH, NPTH, F.Cu at (55.0, 63.1)
- added REF**: NPTH, NPTH, F.Cu at (103.2, 55.7)
- added REF**: NPTH, NPTH, F.Cu at (62.0, 121.1)
- added REF**: NPTH, NPTH, F.Cu at (62.5, 109.7)
- added REF**: NPTH, NPTH, F.Cu at (96.7, 80.0)
- added REF**: NPTH, NPTH, F.Cu at (63.1, 78.0)
- added REF**: NPTH, NPTH, F.Cu at (96.3, 111.6)
- added REF**: NPTH, NPTH, F.Cu at (122.3, 70.5)
- added REF**: NPTH, NPTH, F.Cu at (102.9, 111.0)
- added REF**: NPTH, NPTH, F.Cu at (111.6, 71.2)
- added REF**: NPTH, NPTH, F.Cu at (94.8, 120.4)
- added REF**: NPTH, NPTH, F.Cu at (45.6, 63.3)
- added REF**: NPTH, NPTH, F.Cu at (70.2, 77.3)
- added REF**: NPTH, NPTH, F.Cu at (70.5, 43.7)
- added REF**: NPTH, NPTH, F.Cu at (77.3, 70.6)
- added REF**: NPTH, NPTH, F.Cu at (102.9, 88.0)
- added REF**: NPTH, NPTH, F.Cu at (61.9, 86.0)
- added REF**: NPTH, NPTH, F.Cu at (70.5, 89.3)
- added REF**: NPTH, NPTH, F.Cu at (61.7, 119.7)
- added REF**: NPTH, NPTH, F.Cu at (44.3, 70.6)
- added REF**: NPTH, NPTH, F.Cu at (86.0, 63.7)
- added REF**: NPTH, NPTH, F.Cu at (119.0, 63.7)
- added REF**: NPTH, NPTH, F.Cu at (102.5, 119.7)
- added REF**: NPTH, NPTH, F.Cu at (63.1, 45.0)
- added REF**: NPTH, NPTH, F.Cu at (80.0, 71.1)
- added REF**: NPTH, NPTH, F.Cu at (69.5, 119.7)
- added REF**: NPTH, NPTH, F.Cu at (69.7, 54.4)
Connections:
- net Board_0-Net-(SW1-Pad1) renamed Board_0-Net-(R6-Pad2)
- net Board_1-Net-(SW1-Pad1) renamed Board_1-Net-(R6-Pad2)
- net Board_2-Net-(SW1-Pad1) renamed Board_2-Net-(R6-Pad2)
- net Board_3-Net-(SW1-Pad1) renamed Board_3-Net-(R6-Pad2)
- net Board_4-Net-(SW1-Pad1) renamed Board_4-Net-(R6-Pad2)
- net Board_5-Net-(SW1-Pad1) renamed Board_5-Net-(R6-Pad2)
- net Board_6-Net-(SW1-Pad1) renamed Board_6-Net-(R6-Pad2)
- net Board_7-Net-(SW1-Pad1) renamed Board_7-Net-(R6-Pad2)
- net Board_8-Net-(SW1-Pad1) renamed Board_8-Net-(R6-Pad2)

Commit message: fixing LCSC numbers
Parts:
- C4 (x9), C5 (x9), C6 (x9): value 100uF/6.3V -> DNP
